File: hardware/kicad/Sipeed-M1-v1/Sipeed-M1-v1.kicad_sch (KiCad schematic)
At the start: 165 parts, among them IC1 TROPIC01_chip, J1 USB_C_, J2 JST Connector, J3 Conn_02x20_Odd_Even, J4 Conn_01x09_Pin, J5 Conn_02x03_Odd_Even, Q2 FS8205A, SW1 SW_Push, SW10 SW_Push, SW11 SW_Push, SW12 SW_Push, SW13 SW_Push, SW14 SW_Push, SW15 SW_Push, SW16 SW_Push, SW2 SW_Push, SW3 SW_Push, SW4 SW_Push, SW5 SW_Push, SW6 SW_Push, SW7 SW_Push, SW8 SW_Push, SW9 SW_Push, U1 Sipeed-M1, U2 ESP32-S3-WROOM-1U-N8R8, U3 PAM2401YPADJ, U4 TPS63070RNMR, U5 MCP23017_SO, U6 BQ29700DSER, U7 USBLC6-2SC6, U8 MCP73871

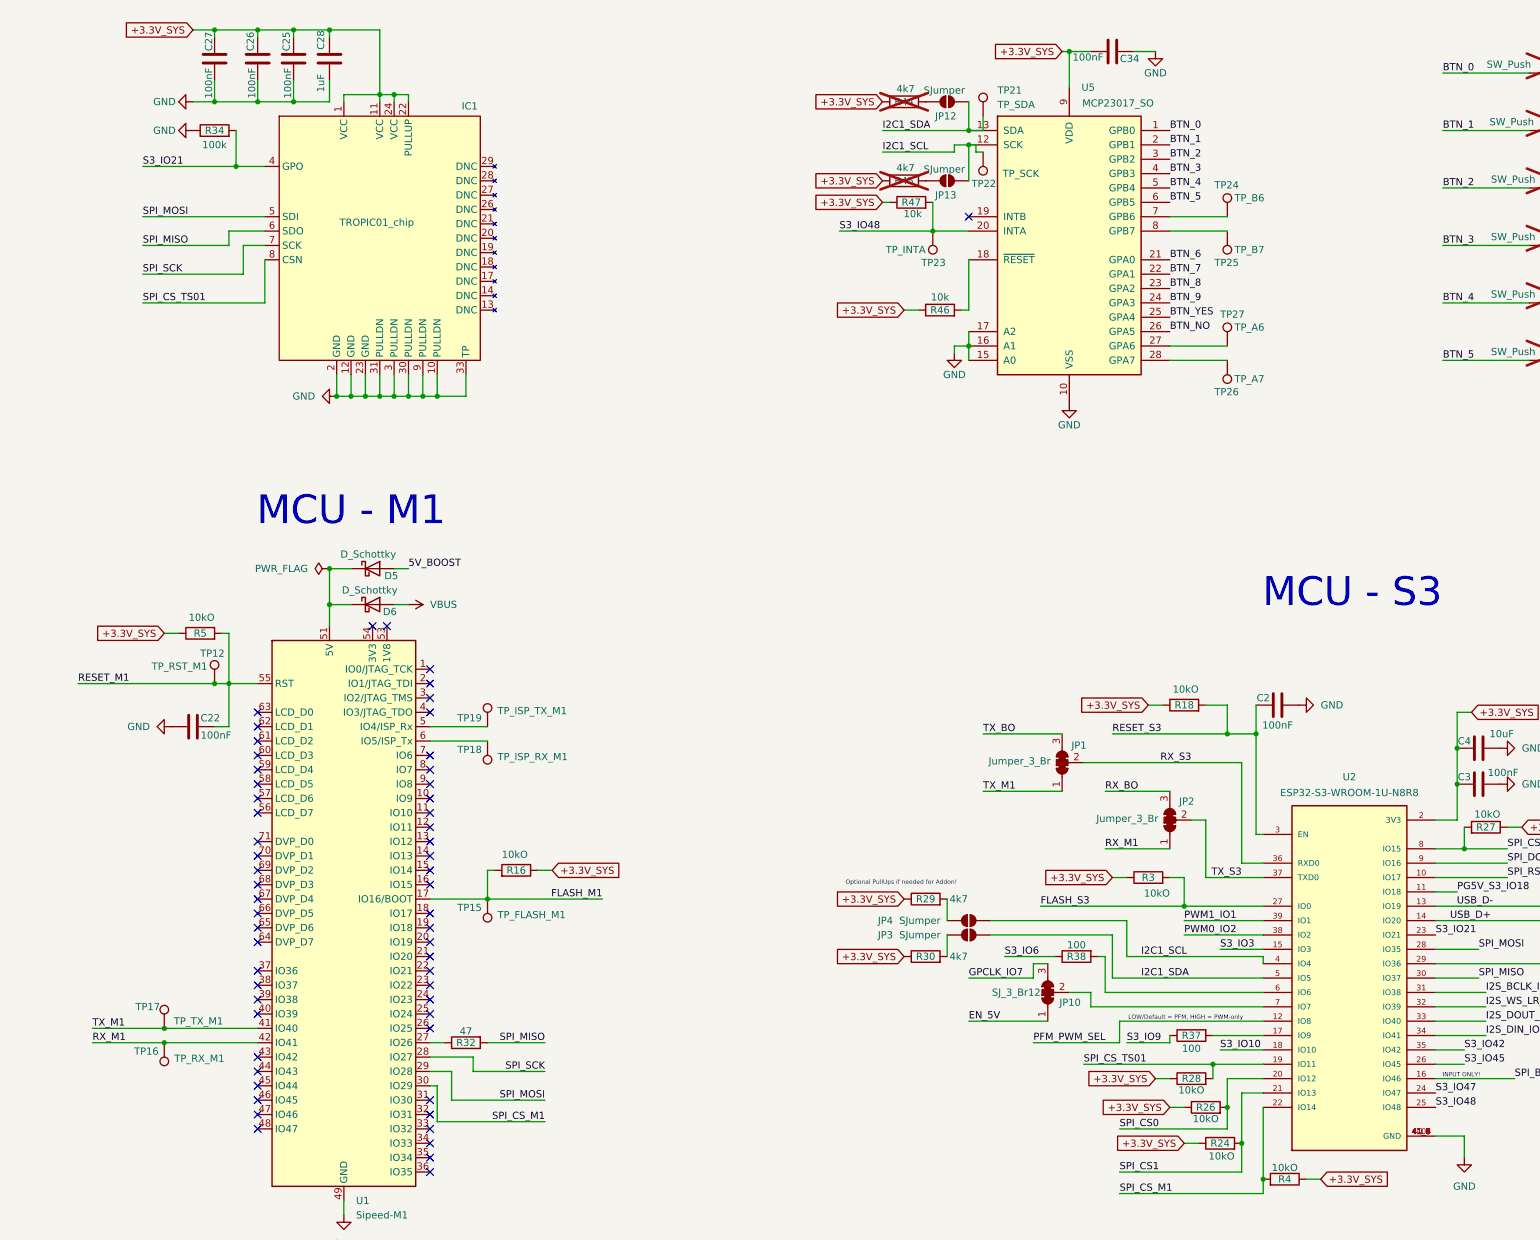
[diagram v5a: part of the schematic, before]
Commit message: cleared some errors for pcb import from schematic(update pcb)
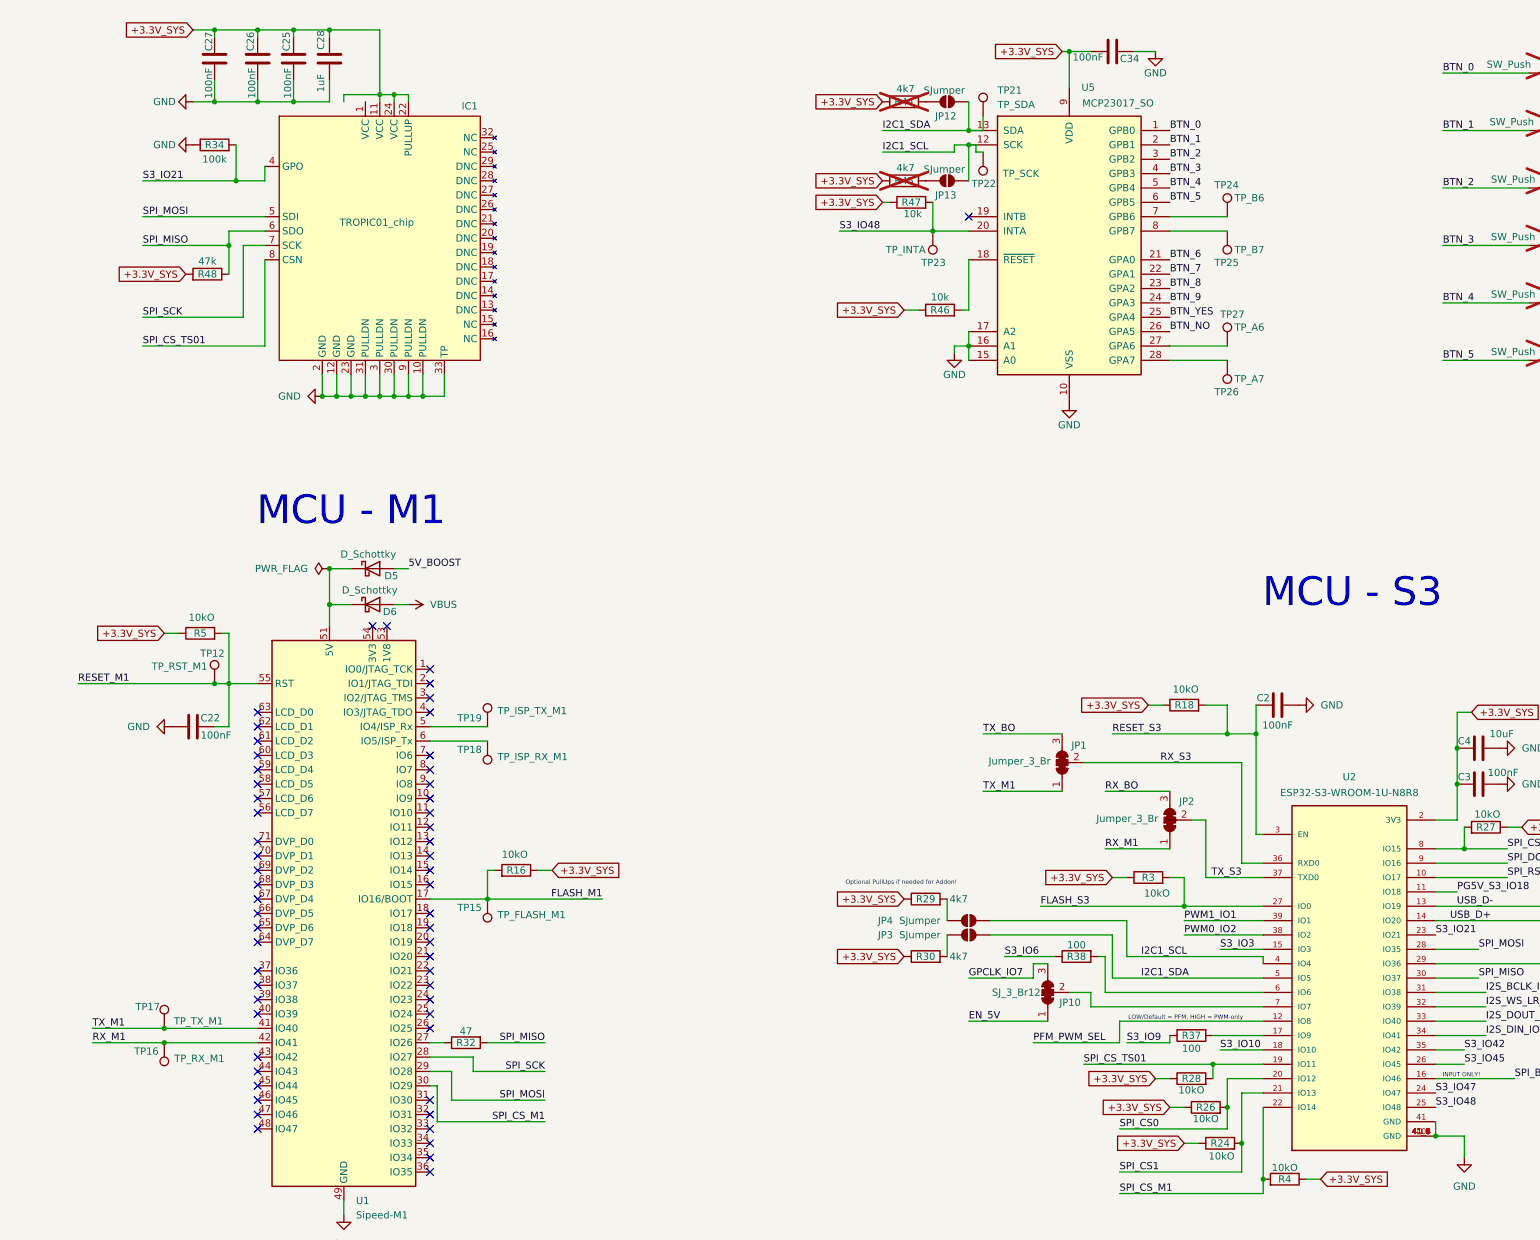
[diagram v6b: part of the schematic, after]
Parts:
- added R48: 47k, Resistor_SMD:R_0603_1608Metric, symbol Device:R
- IC1: footprint _M1_FP_lib:QFN-32-1EP_4x4mm_P0.4mm_EP2.65x2.65mm TROPIC01 -> _M1_FP_lib:TROPIC01 QFN-32-1EP_4x4mm_P0.4mm_EP2.65x2.65mm; symbol _M1_symbols:TROPIC01_chip_pub -> _M1_symbols:TROPIC01
- U2: footprint _M1_FP_lib:XCVR_ESP32-S3-WROOM-1U-N8R8 -> _M1_FP_lib:XCVR_ESP32-S3-WROOM-1U-N8R8-NU; symbol _M1_symbols:ESP32-S3-WROOM-1U-N8R8 -> _M1_symbols:ESP32-S3-WROOM-1U-N8R8-NU41
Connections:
- net +3.3V_SYS: now also R48.2; no longer IC1.1 (VCC)
- net GND: now also U2.41 (GND)
- net SPI_MISO: now also R48.1
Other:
- moved on the sheet: R34

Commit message: Charging IC and USB-C connector review
Charging IC: fix status LEDs, add LED for power good.
Charging IC: add optional through-hole resistor to set charging current.
Charging IC: add thermistor value.
Remove duplicate 10uF decoupling capacitor.
VCC pointing up, GND pointing down.
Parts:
- removed C14: 10uF, Capacitor_SMD:C_1206_3216Metric, symbol Device:C
- added D8: LED_BL, LED_SMD:LED_0603_1608Metric, symbol Device:LED
- added R49: 1K, Resistor_THT:R_Axial_DIN0207_L6.3mm_D2.5mm_P7.62mm_Horizontal, symbol Device:R
- C13: value 10uF -> 4.7uF
- C31: value 22uF -> 4.7uF
- R13, R14: value 1k -> 430
- R15: value 10k -> 430
- TH1: value Therm._NTC -> 10k
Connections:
- net GND: now also C11.2, R49.1; no longer C11.1, D1.1 (K), D2.1 (K)
- net USB_D+: no longer J1.A6 (D+), J1.B6 (D+), U7.3 (I/O2)
- net VBUS: now also C11.1, D1.2 (A), D2.2 (A), D8.2 (A); no longer C11.2, R15.2
- net at R13.2: now also D1.1 (K); no longer D1.2 (A)
- net at R14.2: now also D2.1 (K); no longer D2.2 (A)
- net at R22.2, U8.13 (PROG1): now also R49.2
- new net: J1.A6 (D+), J1.B6 (D+), U7.3 (I/O2)
- new net: D8.1 (K), R15.2
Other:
- note added: "500 mA charging as default desolder R22 and populate R49 for another value"
- moved on the sheet: C10, C11, C12, C31, D1, D2

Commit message: Resolved the Errors from the ERC
Removed several errors at the power lines by defining the ground at
usbc connector as a power source (place power flag). And second error,
define pin in BQ symbol from outpoút to poweroutput as it produced a
error with several output pin connections.
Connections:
- net +3.3V_SYS: now also IC1.1 (VCC)
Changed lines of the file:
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@@
 	)
 	(junction
+		(at 59.69 82.55)
+		(diameter 0)
+		(color 0 0 0 0)
+	)
+	(junction
 		(at 77.47 246.38)
 		(diameter 0)
@@
 	(wire
 		(pts
-			(xy 81.28 193.04) (xy 87.63 193.04)
+			(xy 85.09 193.04) (xy 87.63 193.04)
 		)
 		(stroke
@@
 	(wire
 		(pts
-			(xy 81.28 193.04) (xy 81.28 194.31)
+			(xy 85.09 193.04) (xy 85.09 194.31)
 		)
 		(stroke
@@
 	(wire
 		(pts
-			(xy 57.15 82.55) (xy 60.96 82.55)
+			(xy 57.15 82.55) (xy 59.69 82.55)
 		)
 		(stroke
@@
 	(wire
 		(pts
+			(xy 59.69 82.55) (xy 60.96 82.55)
+		)
+		(stroke
+			(width 0)
+			(type default)
+		)
+	)
+	(wire
+		(pts
 			(xy 240.03 328.93) (xy 243.84 328.93)
 		)
@@
 	)
 	(symbol
-		(lib_id "power:PWR_FLAG")
-		(at 454.66 382.27 0)
-		(unit 1)
-		(exclude_from_sim no)
-		(in_bom yes)
-		(on_board yes)
-		(dnp no)
-		(fields_autoplaced yes)
-		(property "Reference" "#FLG03"
-			(at 454.66 380.365 0)
-			(effects
-				(font
-					(size 1.27 1.27)
-				)
-				(hide yes)
-			)
-		)
-		(property "Value" "PWR_FLAG"
-			(at 454.66 377.19 0)
-			(effects
-				(font
-					(size 1.27 1.27)
-				)
-			)
-		)
-		(property "Footprint" ""
-			(at 454.66 382.27 0)
-			(effects
-				(font
-					(size 1.27 1.27)
-				)
-				(hide yes)
-			)
-		)
-		(property "Datasheet" "~"
-			(at 454.66 382.27 0)
-			(effects
-				(font
-					(size 1.27 1.27)
-				)
-				(hide yes)
-			)
-		)
-		(property "Description" "Special symbol for telling ERC where power comes from"
-			(at 454.66 382.27 0)
-			(effects
-				(font
-					(size 1.27 1.27)
-				)
-				(hide yes)
-			)
-		)
-		(pin "1"
-		)
-		(instances
-			(project ""
-				(path "/2cec4f7a-7b92-4a21-be0b-2bac184578cb"
-					(reference "#FLG03")
-					(unit 1)
-				)
-			)
-		)
-	)
-	(symbol
 		(lib_id "Jumper:SolderJumper_3_Bridged123")
 		(at 205.74 351.79 90)
@@
 	)
 	(symbol
+		(lib_id "power:PWR_FLAG")
+		(at 59.69 82.55 0)
+		(unit 1)
+		(exclude_from_sim no)
+		(in_bom yes)
+		(on_board yes)
+		(dnp no)
+		(property "Reference" "#FLG03"
+			(at 59.69 80.645 0)
+			(effects
+				(font
+					(size 1.27 1.27)
+				)
+				(hide yes)
+			)
+		)
+		(property "Value" "PWR_FLAG"
+			(at 63.5 79.248 0)
+			(effects
+				(font
+					(size 1.27 1.27)
+				)
+			)
+		)
+		(property "Footprint" ""
+			(at 59.69 82.55 0)
+			(effects
+				(font
+					(size 1.27 1.27)
+				)
+				(hide yes)
+			)
+		)
+		(property "Datasheet" "~"
+			(at 59.69 82.55 0)
+			(effects
+				(font
+					(size 1.27 1.27)
+				)
+				(hide yes)
+			)
+		)
+		(property "Description" "Special symbol for telling ERC where power comes from"
+			(at 59.69 82.55 0)
+			(effects
+				(font
+					(size 1.27 1.27)
+				)
+				(hide yes)
+			)
+		)
+		(pin "1"
+		)
+		(instances
+			(project "Sipeed-M1-v1"
+				(path "/2cec4f7a-7b92-4a21-be0b-2bac184578cb"
+					(reference "#FLG03")
+					(unit 1)
+				)
+			)
+		)
+	)
+	(symbol
 		(lib_id "power:GND")
 		(at 77.47 246.38 270)
@@
 					(unit 1)
 				)
-			)
-		)
-	)
-	(symbol
-		(lib_id "power:GND")
-		(at 454.66 382.27 0)
-		(unit 1)
-		(exclude_from_sim no)
-		(in_bom yes)
-		(on_board yes)
-		(dnp no)
-		(fields_autoplaced yes)
-		(property "Reference" "#PWR057"
-			(at 454.66 388.62 0)
-			(effects
-				(font
-					(size 1.27 1.27)
-				)
-				(hide yes)
-			)
-		)
-		(property "Value" "GND"
-			(at 454.66 387.35 0)
-			(effects
-				(font
-					(size 1.27 1.27)
-				)
-			)
-		)
-		(property "Footprint" ""
-			(at 454.66 382.27 0)
-			(effects
-				(font
-					(size 1.27 1.27)
-				)
-				(hide yes)
-			)
-		)
-		(property "Datasheet" ""
-			(at 454.66 382.27 0)
-			(effects
-				(font
-					(size 1.27 1.27)
-				)
-				(hide yes)
-			)
-		)
-		(property "Description" "Power symbol creates a global label with name \"GND\" , ground"
-			(at 454.66 382.27 0)
-			(effects
-				(font
-					(size 1.27 1.27)
-				)
-				(hide yes)
-			)
-		)
-		(pin "1"
-		)
-		(instances
-			(project ""
-				(path "/2cec4f7a-7b92-4a21-be0b-2bac184578cb"
-					(reference "#PWR057")
-					(unit 1)
-				)
